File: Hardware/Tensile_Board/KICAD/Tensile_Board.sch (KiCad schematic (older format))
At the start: 25 parts, among them J1 Conn_02x05_Odd_Even, J11 Screw_Terminal_01x04, J2 Conn_02x05_Odd_Even, J3 Conn_02x05_Odd_Even, J4 Conn_02x05_Odd_Even, J5 Micro_SD_Card, J6 Main_Power, J9 Grounding, U1 AMS1117-5.0, U2 AMS1117-3.3, U20 APM4953, U3 DS3231M

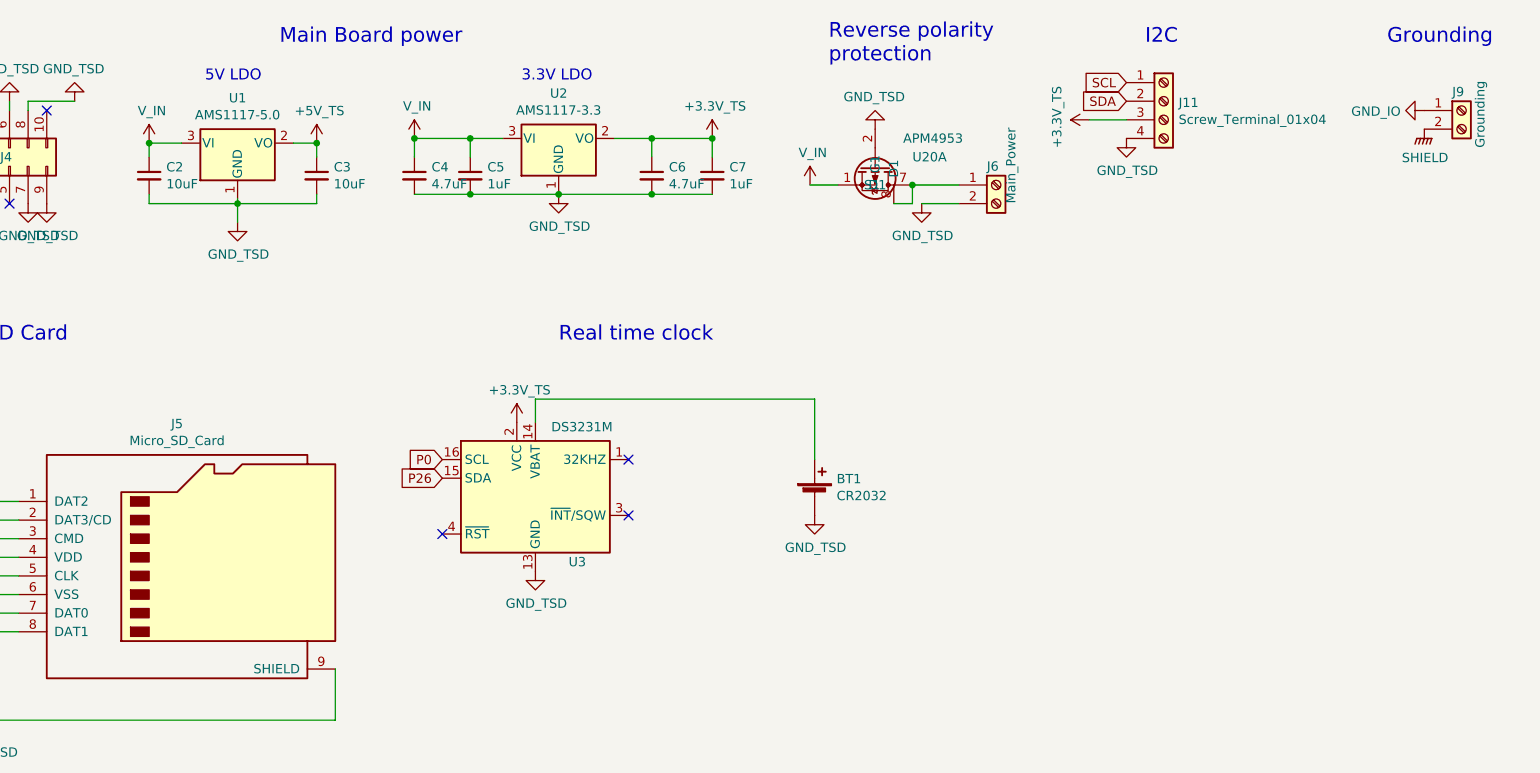
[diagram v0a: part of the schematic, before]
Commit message: started changing LDO's to buck regulators
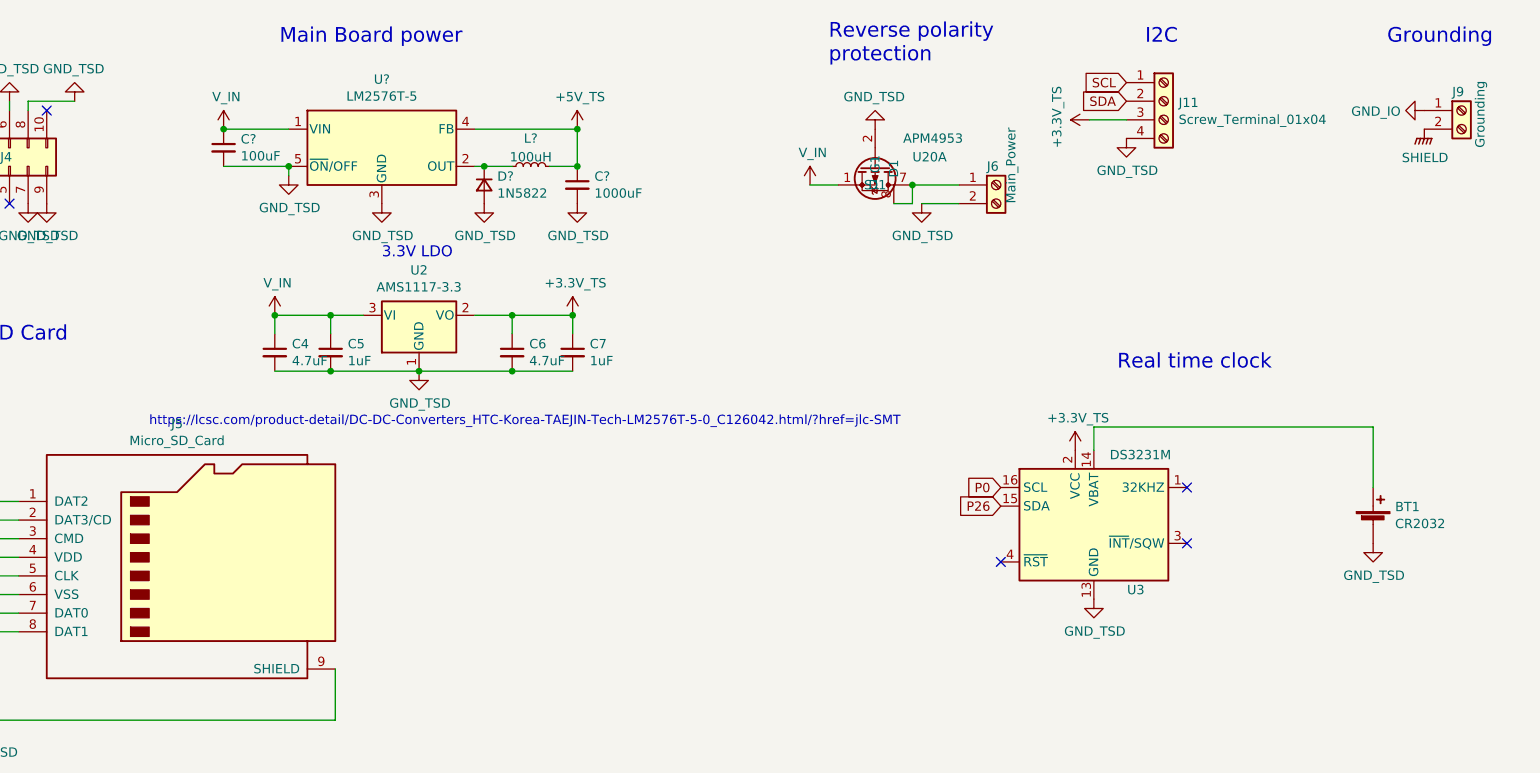
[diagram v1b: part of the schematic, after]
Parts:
- removed C2, C3: 10uF, Capacitor_SMD:C_0805_2012Metric, symbol Device:C_Small
- removed U1: AMS1117-5.0, Package_TO_SOT_SMD:SOT-223-3_TabPin2, symbol Regulator_Linear:AMS1117-5.0
- added C?: 100uF, Capacitor_SMD:C_0805_2012Metric, symbol Device:C_Small
- added C?: 1000uF, Capacitor_SMD:C_0805_2012Metric, symbol Device:C_Small
- added D?: 1N5822, symbol Device:D_Small
- added L?: 100uH, symbol Device:L_Small
- added U?: LM2576T-5, Package_TO_SOT_THT:TO-220-5_Vertical, symbol Regulator_Switching:LM2576T-5
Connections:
- net +5V_TS: now also C?.1, L?.2, U?.4 (FB)
- net GND_TSD: now also C?.2, C?.2, D?.2 (A), U?.3 (GND), U?.5 (~ON~/OFF)
- net V_IN: now also C?.1, U?.1 (VIN)
- new net: D?.1 (K), L?.1, U?.2 (OUT)
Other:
- note added: "https://lcsc.com/product-detail/DC-DC-Converters_HTC-Korea-TAEJIN-Tech-LM2576T-5-0_C126042.html/?href=jlc-SMT"
- note removed: "5V LDO"
- moved on the sheet: BT1, C4, C5, C6, C7, U2, U3

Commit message: groundwork for p2
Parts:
- removed C4, C6: 4.7uF, Capacitor_SMD:C_0805_2012Metric, symbol Device:C_Small
- removed C5, C7: 1uF, Capacitor_SMD:C_0603_1608Metric, symbol Device:C_Small
- removed C?: 100uF, Capacitor_SMD:C_0805_2012Metric, symbol Device:C_Small
- removed C?: 1000uF, Capacitor_SMD:C_0805_2012Metric, symbol Device:C_Small
- removed D?: 1N5822, symbol Device:D_Small
- removed L?: 100uH, symbol Device:L_Small
- removed U2: AMS1117-3.3, Package_TO_SOT_SMD:SOT-223-3_TabPin2, symbol Regulator_Linear:AMS1117-3.3
- removed U?: LM2576T-5, Package_TO_SOT_THT:TO-220-5_Vertical, symbol Regulator_Switching:LM2576T-5
- added C? (x2): 470uF, symbol Device:C_Small
- added C?: 180uF, symbol Device:C_Small
- added C?: 330uF, symbol Device:C_Small
- added D? (x2): SS36, symbol Device:D_Schottky_Small
- added L?: 68uH/3A, symbol Device:L_Small
- added L?: 47uH/3A, symbol Device:L_Small
- added U?: XL1509-5V, symbol Tensile_Board:XL1509
- added U?: XL1509-3.3V, symbol Tensile_Board:XL1509
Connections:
- net +3V3_TS: now also C?.1, L?.2, U?.3 (FDB)
- net +5V_TS: now also C?.1, L?.2, U?.3 (FDB)
- net GND_TSD: now also C?.2, C?.2, C?.2, C?.2, D?.2 (A), D?.2 (A), U?.4 (~ON), U?.4 (~ON), U?.5 (GND), U?.5 (GND), U?.6 (GND), U?.6 (GND), U?.7 (GND), U?.7 (GND), U?.8 (GND), U?.8 (GND)
- net V_IN: now also C?.1, C?.1, U?.1 (VIN), U?.1 (VIN)
- new net: D?.1 (K), L?.1, U?.2 (OUT) (x2)
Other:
- note removed: "3.3V LDO"
- note removed: "https://lcsc.com/product-detail/DC-DC-Converters_HTC-Korea-TAEJIN-Tech-LM2576T-5-0_C126042.html/?href=jlc-SMT"
